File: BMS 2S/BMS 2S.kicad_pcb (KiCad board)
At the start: 2 copper layers, 64 x 36 mm, 26 parts, among them J1 Screw_Terminal_01x01, J2 Screw_Terminal_01x01, J3 Screw_Terminal_01x01, J4 Screw_Terminal_01x01, J5 Screw_Terminal_01x01, J6 Screw_Terminal_01x01, Q1 DMG2302UK-7, Q2 DMG2302UK-7, Q3 DMG2302UK-7, Q4 DMG2302UK-7, U1 S-8252AAZ-M6T1U, U2 S-8252AAZ-M6T1U

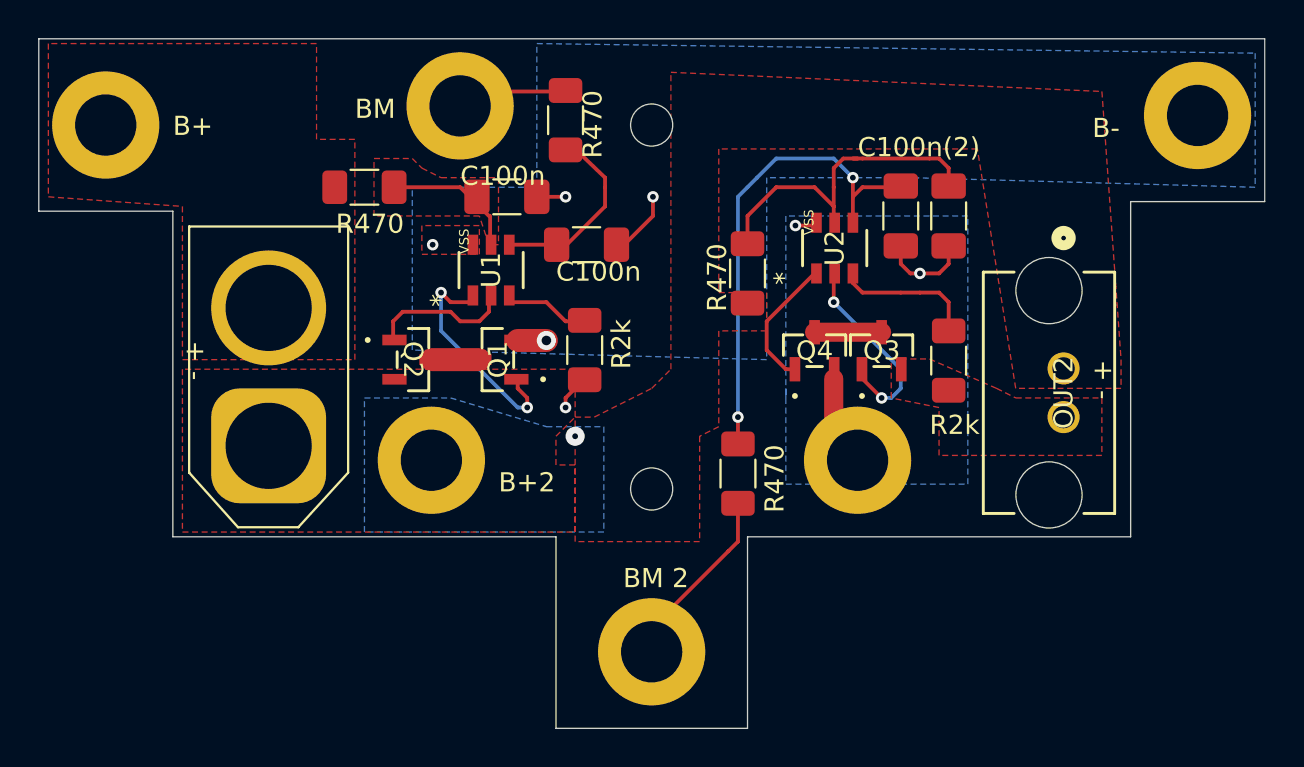
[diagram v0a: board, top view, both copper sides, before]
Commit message: BMS 2S, ajustement du design
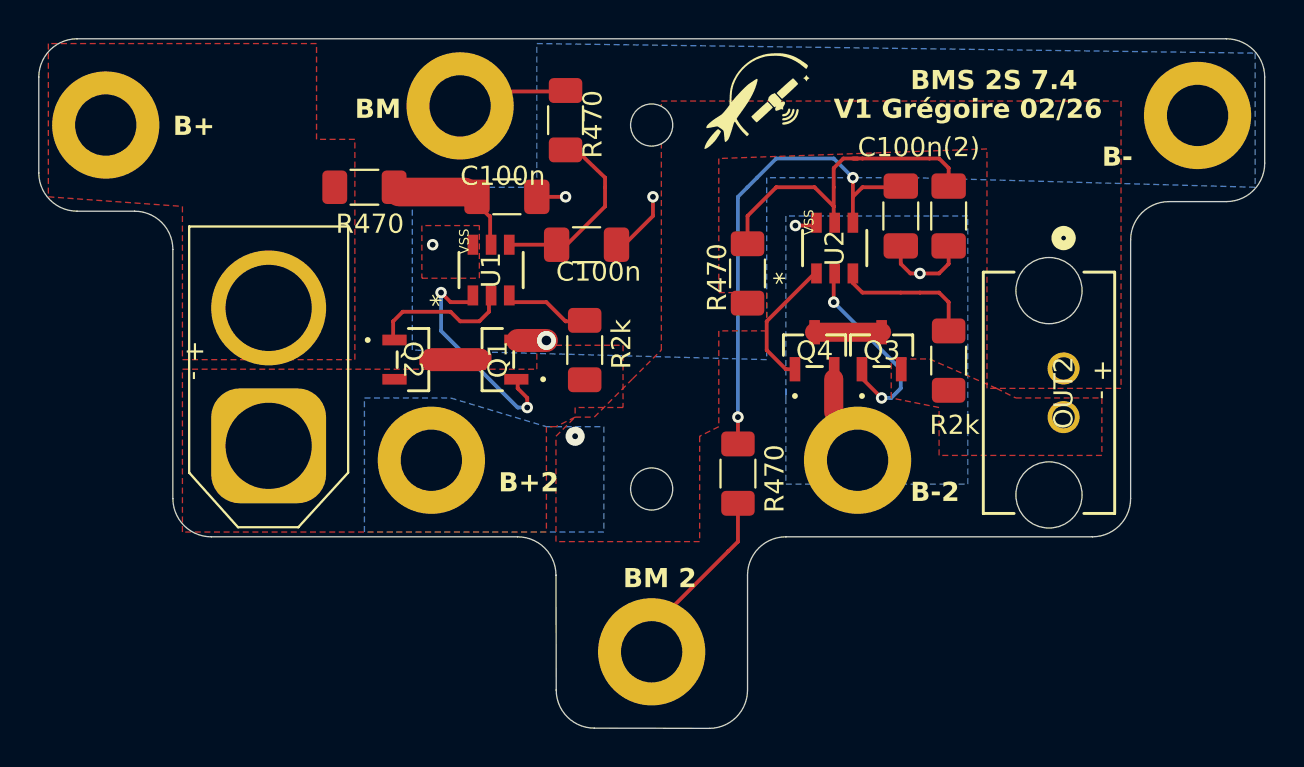
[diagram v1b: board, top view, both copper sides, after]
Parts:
- added G***: LOGO, Library:logoS, F.Cu at (111.5, 76.5)
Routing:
- net Out-: vias 1 -> 0
- removed copper zone on F.Cu, net Net-(U1-VDD)
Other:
- outline, holes or cut-outs redrawn
- board text added: "B-2"
- board text added: "BMS 2S 7.4"
- board text added: "V1 Grégoire 02/26"

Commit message: BMS 2S : Amélioration des paths et fix de bugs de silkscreen.
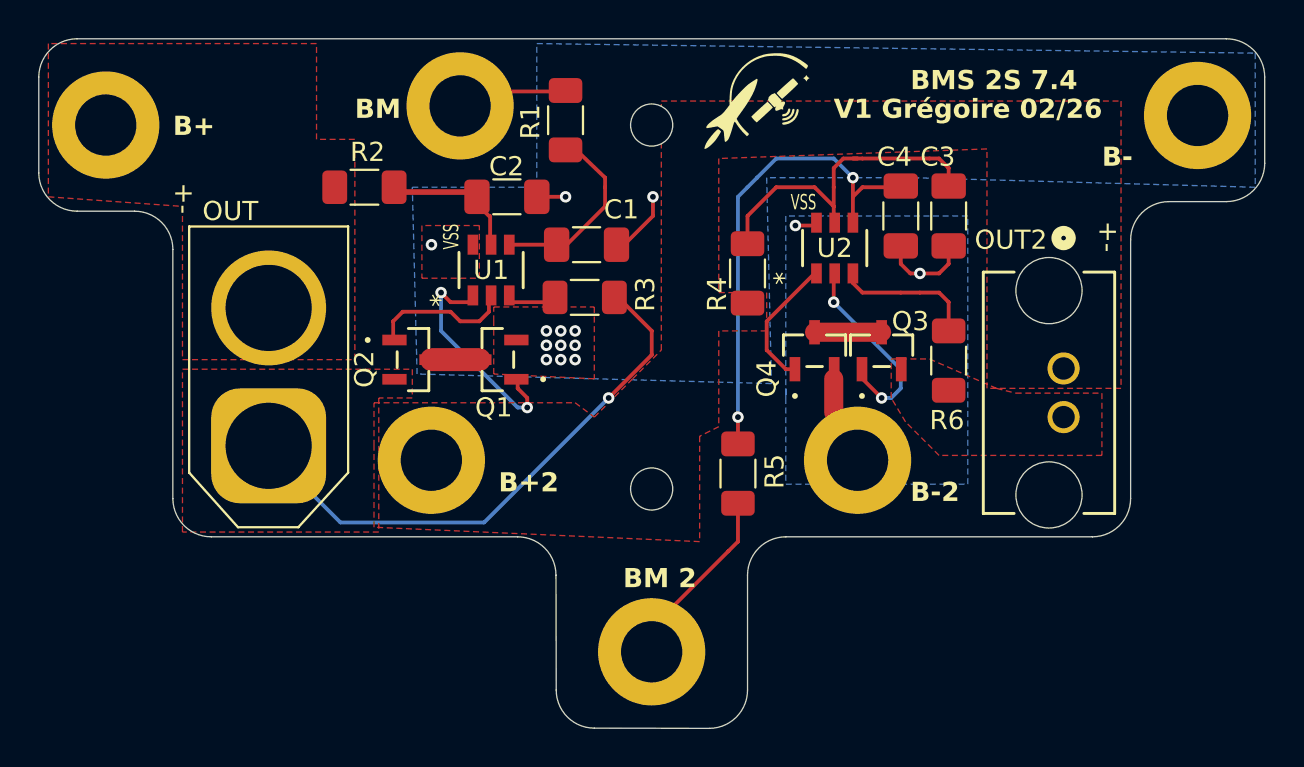
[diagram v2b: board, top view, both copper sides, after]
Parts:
- moved R3 2.75 mm to (102.5, 86.8), turned to 180 degrees
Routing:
- net Out-: vias 0 -> 1
- net Out+ B+2: vias 1 -> 0
- net B-: vias 4 -> 12
- removed copper zone on B.Cu, net Out+ B+2
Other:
- board text added: "+-"
- board text added: "C1"
- board text added: "C2"
- board text added: "C4 C3"
- board text added: "OUT"
- board text added: "R1"
- board text added: "R2"
- board text added: "R3"
- board text added: "R4"
- board text added: "R5"
- board text added: "R6"
- board text removed: "+ -"
- board text removed: "C100n"
- board text removed: "C100n(2)"
- board text removed: "R2k"
- board text removed: "R470"

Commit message: Changement des nmos du circuit principal
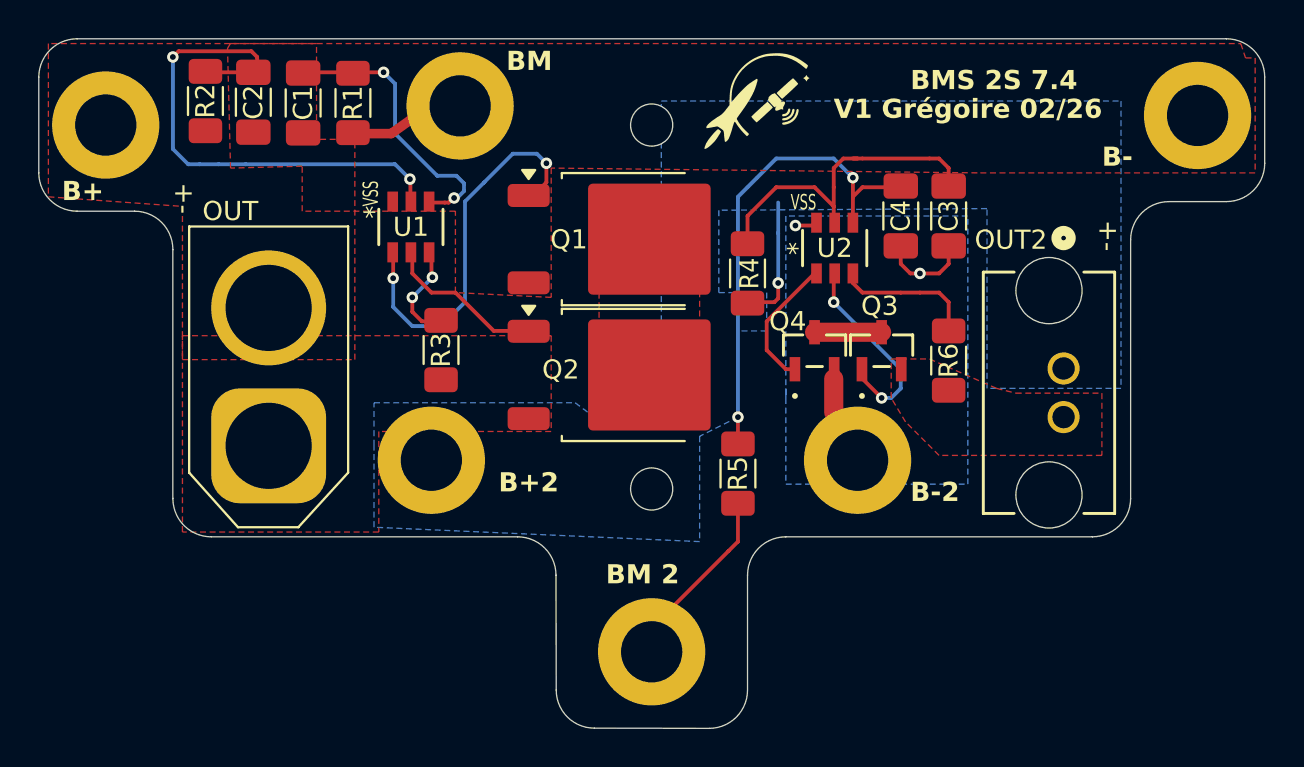
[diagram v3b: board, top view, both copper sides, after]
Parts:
- Q1, Q2: value DMG2302UK-7 -> ZXMN4A06K; footprint BMS_footprints:SOT23_DMG230_DIO -> Package_TO_SOT_SMD:TO-252-2
- moved C1 16.5 mm to (87.8, 76.6), turned to -90 degrees
- moved C2 14.1 mm to (85.2, 76.6), turned to -90 degrees
- moved R1 11.1 mm to (90.4, 76.6), turned to -90 degrees
- moved Q2 11.1 mm to (104.6, 90.8), turned to 0 degrees
- moved R2 9.44 mm to (82.7, 76.5), turned to -90 degrees
- moved Q1 9.15 mm to (104.6, 83.7), turned to 0 degrees
- moved R3 7.99 mm to (95.0, 89.5), turned to 90 degrees
- moved U1 4.75 mm to (93.4, 83.1)
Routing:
- net Out-: vias 1 -> 0
- net Out+ B+2: vias 0 -> 1
- net Net-(U1-VM): vias 0 -> 2
- net Net-(U1-VDD): vias 0 -> 2
- net Net-(U1-VC): vias 0 -> 2
- net B-: vias 12 -> 0
- added copper zone on F.Cu, net Net-(Q1-D)
- added copper zone on B.Cu, net Out+ B+2
- removed copper zone on B.Cu, net B-
- removed copper zone on F.Cu, net Out+ B+2
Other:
- board text removed: "C1"
- board text removed: "C2"
- board text removed: "C4 C3"
- board text removed: "R1"
- board text removed: "R2"
- board text removed: "R3"
- board text removed: "R4"
- board text removed: "R5"
- board text removed: "R6"

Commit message: commande pcbway
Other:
- board text removed: "VSS"
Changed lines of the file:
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@@
 		(tags "resistor handsolder")
 		(property "Reference" "R2"
-			(at 0 0 90)
+			(at 3.237187 0.019262 180)
 			(layer "F.SilkS")
 			(effects
@@
 		(tags "S-8252AAZ-M6T1U ")
 		(property "Reference" "U1"
-			(at 0 0 0)
+			(at 0 2.820621 0)
 			(unlocked yes)
 			(layer "F.SilkS")
@@
 		)
 		(fp_text user "*"
-			(at 0.774351 -1.925649 90)
+			(at -1.496248 -1.663185 90)
 			(unlocked yes)
 			(layer "F.SilkS")
@@
 		(tags "S-8252AAZ-M6T1U ")
 		(property "Reference" "U2"
-			(at 0 0 0)
+			(at 2.805143 -0.054999 0)
 			(unlocked yes)
 			(layer "F.SilkS")
@@
 		)
 		(fp_text user "*"
-			(at -0.024351 -1.949999 90)
+			(at -1.270953 -1.753372 90)
 			(layer "F.SilkS")
 			(effects
@@
 		(tags "capacitor handsolder")
 		(property "Reference" "C3"
-			(at 0 0 270)
+			(at -3.074927 0.020467 0)
 			(layer "F.SilkS")
 			(effects
@@
 		(tags "capacitor handsolder")
 		(property "Reference" "C4"
-			(at 0 0 270)
+			(at -3.086845 0.047171 0)
 			(layer "F.SilkS")
 			(effects
@@
 		(tags "resistor handsolder")
 		(property "Reference" "R3"
-			(at 0 0 90)
+			(at 0 -1.810803 90)
 			(layer "F.SilkS")
 			(effects
@@
 		(tags "DPAK TO-252 DPAK-3 TO-252-3 SOT-428")
 		(property "Reference" "Q2"
-			(at -3.365 -0.275 0)
+			(at -2.415484 4.29406 0)
 			(layer "F.SilkS")
 			(effects
@@
 		(tags "resistor handsolder")
 		(property "Reference" "R1"
-			(at 0 0 90)
+			(at 3.137187 -0.080738 180)
 			(layer "F.SilkS")
 			(effects
@@
 		(tags "resistor handsolder")
 		(property "Reference" "R4"
-			(at 0 -0.1 270)
+			(at -3.046657 -0.013181 0)
 			(layer "F.SilkS")
 			(effects
@@
 		(tags "resistor handsolder")
 		(property "Reference" "R6"
-			(at 0 0 90)
+			(at -3.155488 0 180)
 			(layer "F.SilkS")
 			(effects
@@
 		(tags "capacitor handsolder")
 		(property "Reference" "C2"
-			(at 0 0 90)
+			(at 3.174687 0.019262 180)
 			(layer "F.SilkS")
 			(effects
@@
 		(tags "DMG2302UK-7 ")
 		(property "Reference" "Q4"
-			(at -1.4 -1.5348 0)
+			(at -2.87451 0.021668 0)
 			(unlocked yes)
 			(layer "F.SilkS")
@@
 		(tags "capacitor handsolder")
 		(property "Reference" "C1"
-			(at 0 0 90)
+			(at 3.137187 0.002289 180)
 			(layer "F.SilkS")
 			(effects
@@
 		(tags "DMG2302UK-7 ")
 		(property "Reference" "Q3"
-			(at -0.1 -2.3348 0)
+			(at -0.127277 -2.49709 0)
 			(unlocked yes)
 			(layer "F.SilkS")
@@
 		(tags "DPAK TO-252 DPAK-3 TO-252-3 SOT-428")
 		(property "Reference" "Q1"
-			(at -2.94 0.02 0)
+			(at -2.14732 -4.410815 0)
 			(layer "F.SilkS")
 			(effects
@@
 	)
 	(gr_text "B+2\n"
-		(at 98 97 0)
+		(at 97.506642 97.534354 0)
 		(layer "F.SilkS")
 		(effects
@@
 		)
 	)
-	(gr_text "VSS"
-		(at 113.25 82.25 0)
-		(layer "F.SilkS")
-		(effects
-			(font
-				(size 0.8 0.5)
-				(thickness 0.08)
-			)
-			(justify left bottom)
-		)
-	)
 	(gr_text "BM 2\n"
 		(at 103.6 101.8 0)
@@
 			)
 			(justify left bottom)
-		)
-	)
-	(gr_text "VSS"
-		(at 91.8 82 90)
-		(layer "F.SilkS")
-		(effects
-			(font
-				(size 0.8 0.5)
-				(thickness 0.08)
-			)
-			(justify left bottom)
